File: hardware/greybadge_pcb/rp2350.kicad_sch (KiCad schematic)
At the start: 35 parts, among them J6 USB_C_Receptacle_USB2.0, SW10 SW_Push, SW9 SW_Push, U6 W25Q128JVS, U7 RP2350_60QFN, Y1 12Mhz

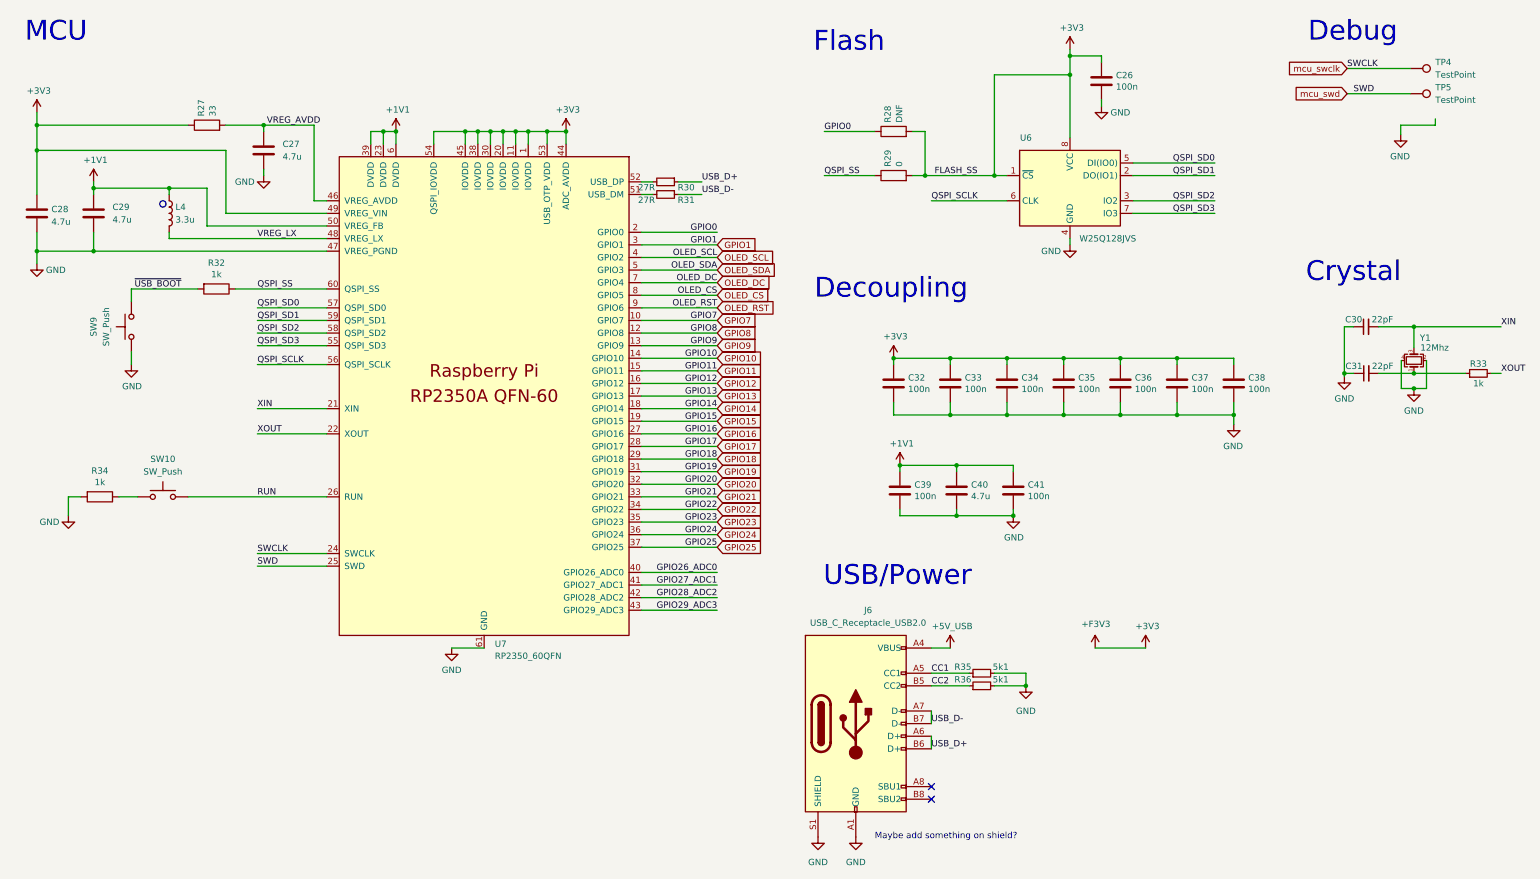
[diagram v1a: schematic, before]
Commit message: Fix: battery/power and clean up silkscreen references
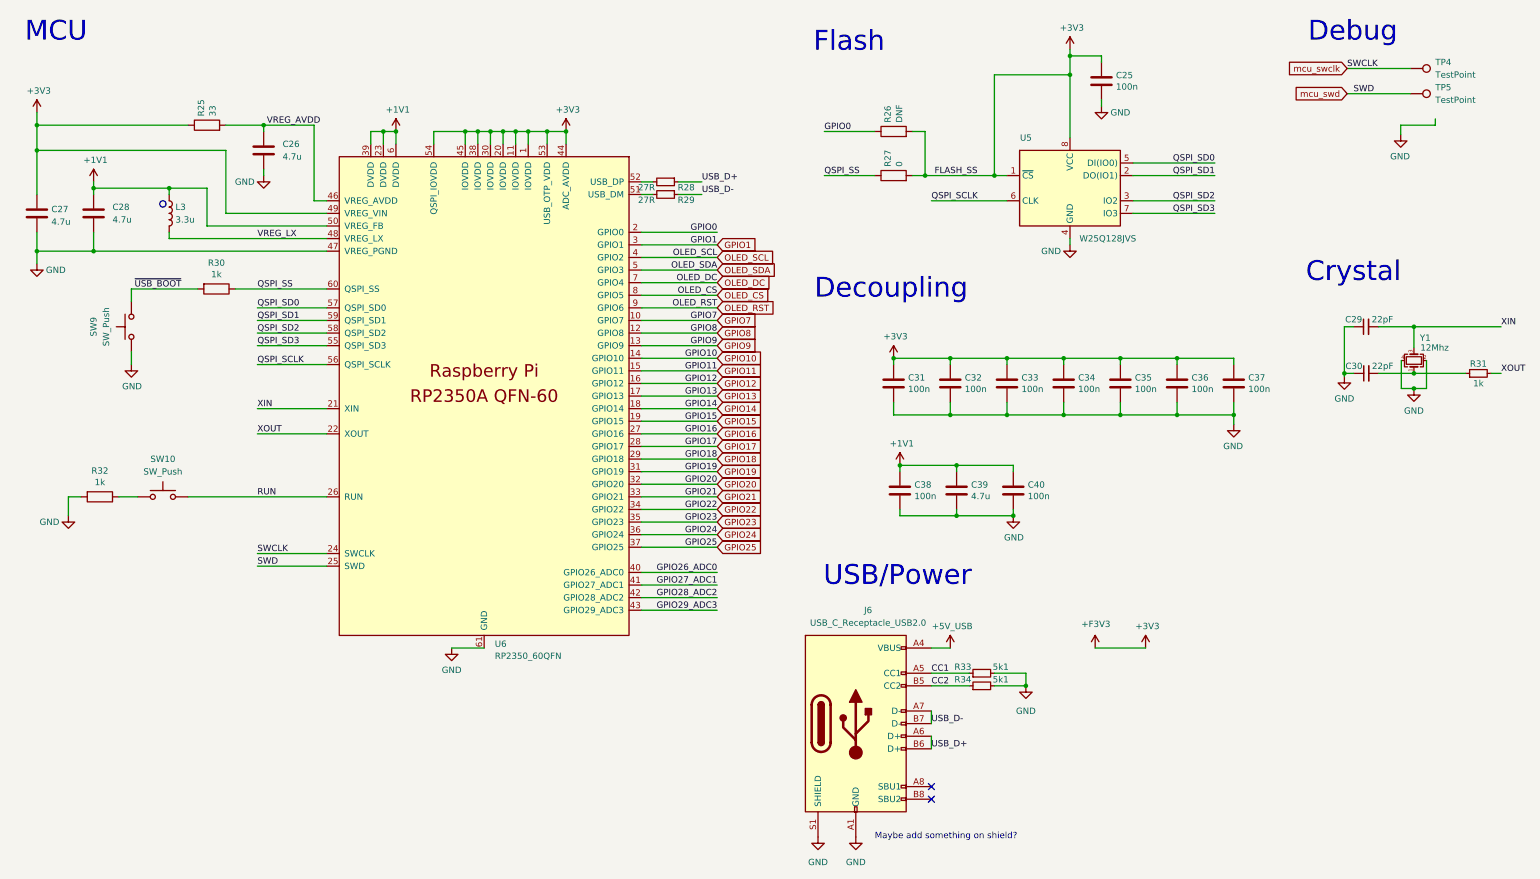
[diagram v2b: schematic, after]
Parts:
- renumbered C26 to C25, C27 to C26, C28 to C27, C29 to C28, C30 to C29, C31 to C30, C32 to C31, C33 to C32, C34 to C33, C35 to C34, C36 to C35, C37 to C36, C38 to C37, C39 to C38, C40 to C39, C41 to C40, L4 to L3, R27 to R25, R28 to R26, R29 to R27, R30 to R28, R31 to R29, R32 to R30, R33 to R31, R34 to R32, R35 to R33, R36 to R34, U6 to U5, U7 to U6

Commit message: Add onboard oled (incomplete)
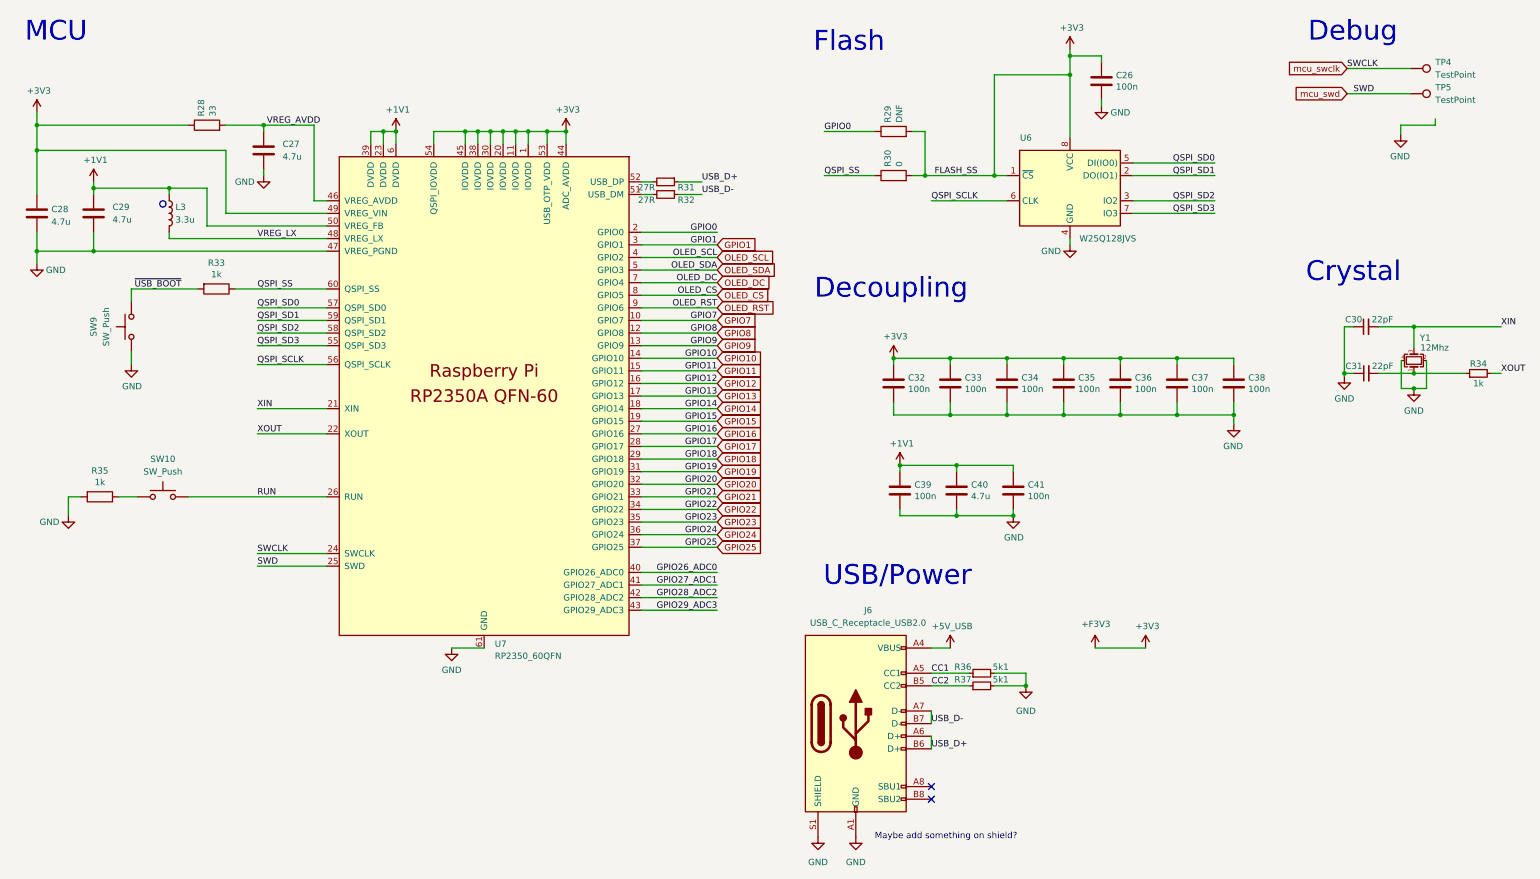
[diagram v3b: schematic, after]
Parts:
- U7: renamed from U6; footprint footprints:RP2350-QFN-60-1EP_7x7_P0.4mm_EP3.4x3.4mm_ThermalVias -> custom:RP2350-QFN-60-1EP_7x7_P0.4mm_EP3.4x3.4mm_ThermalVias
- renumbered C25 to C26, C26 to C27, C27 to C28, C28 to C29, C29 to C30, C30 to C31, C31 to C32, C32 to C33, C33 to C34, C34 to C35, C35 to C36, C36 to C37, C37 to C38, C38 to C39, C39 to C40, C40 to C41, R25 to R28, R26 to R29, R27 to R30, R28 to R31, R29 to R32, R30 to R33, R31 to R34, R32 to R35, R33 to R36, R34 to R37, U5 to U6
